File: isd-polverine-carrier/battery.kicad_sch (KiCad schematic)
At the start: 26 parts, among them J2 Jack-DC, Q2 Q_PMOS, U2 CN3791, U3 ACS712xLCTR-05B, U4 ACS712xLCTR-05B

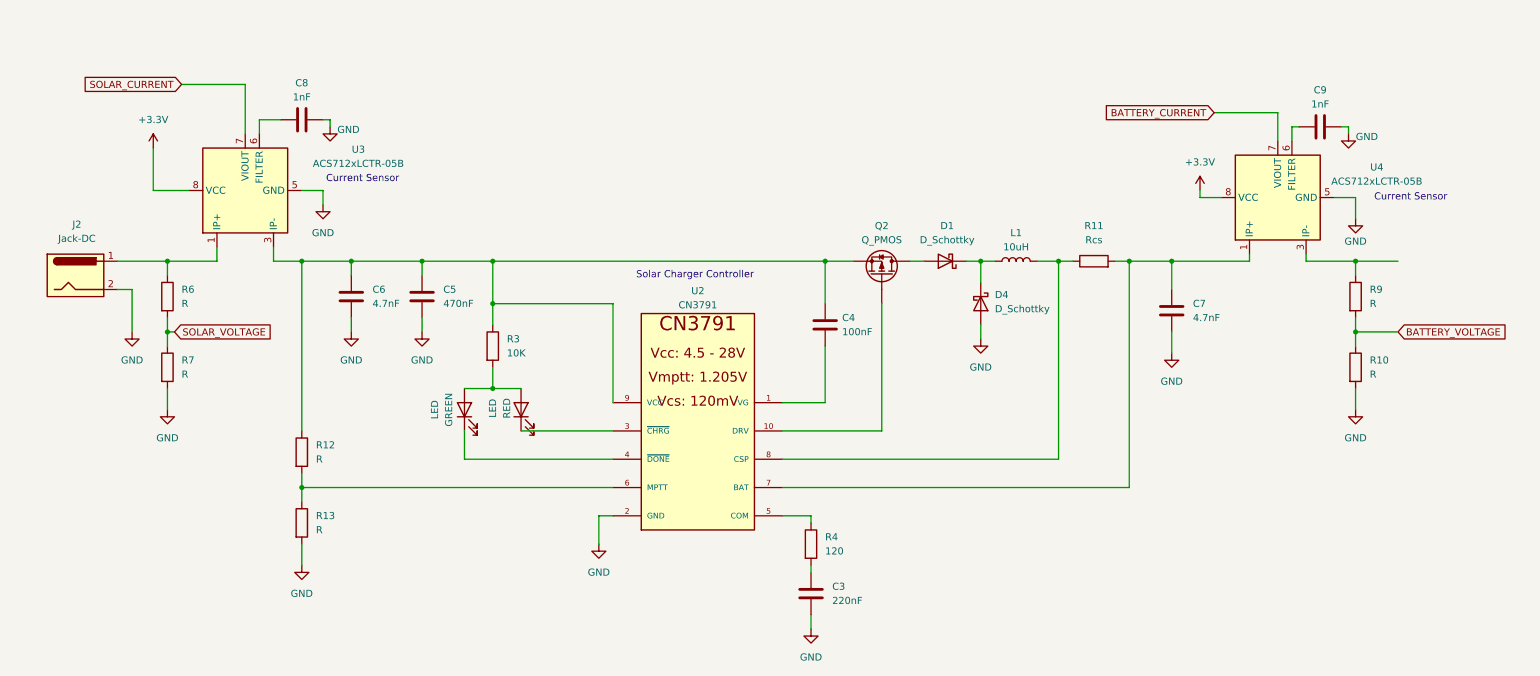
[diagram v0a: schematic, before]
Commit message: Added P Mos to solar charger controller for load sharing
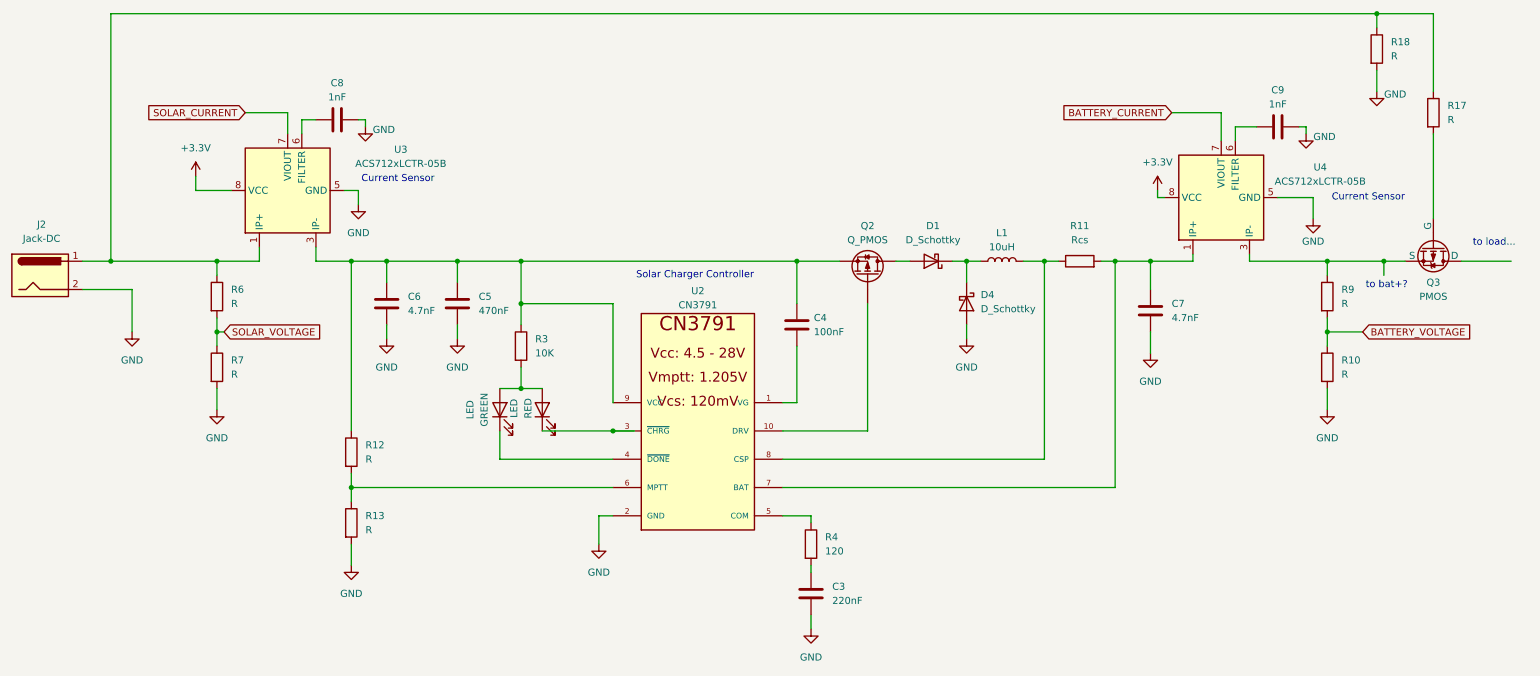
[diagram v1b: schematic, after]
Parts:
- added Q3: PMOS, symbol Simulation_SPICE:PMOS
- added R17, R18: R, symbol Device:R
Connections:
- net GND: now also R18.2
- net at J2.1, R6.1, U3.1 (IP+)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: now also R17.1, R18.1
- net at R9.1, U4.3 (IP-), U4.4 (IP-): now also Q3.3 (S)
- new net: Q3.2 (G), R17.2
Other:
- note added: "to bat+?"
- note added: "to load..."
- moved on the sheet: C4, C5, C6, C7, C8, C9, D1, D4, GREEN, J2, L1, Q2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
